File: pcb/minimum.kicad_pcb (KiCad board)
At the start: 4 copper layers, 16 x 20 mm, 31 parts, among them J1 DX07P024MJ1R1500, U1 RP2040, U2 SCD4x, U3 W25Q16JVUXIQ, U4 XCL220, Y1 C2E-12.000-18-1020-X-R

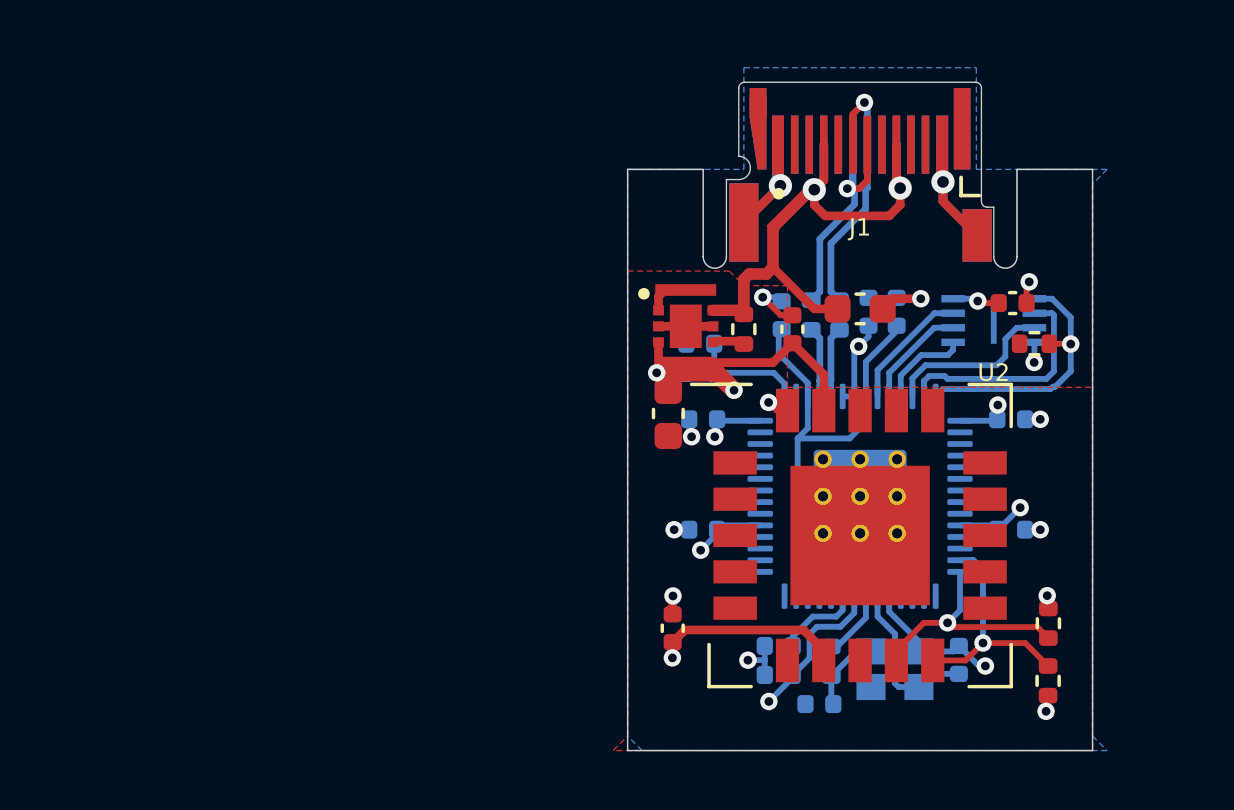
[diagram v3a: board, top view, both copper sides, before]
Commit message: adding led and push button libs
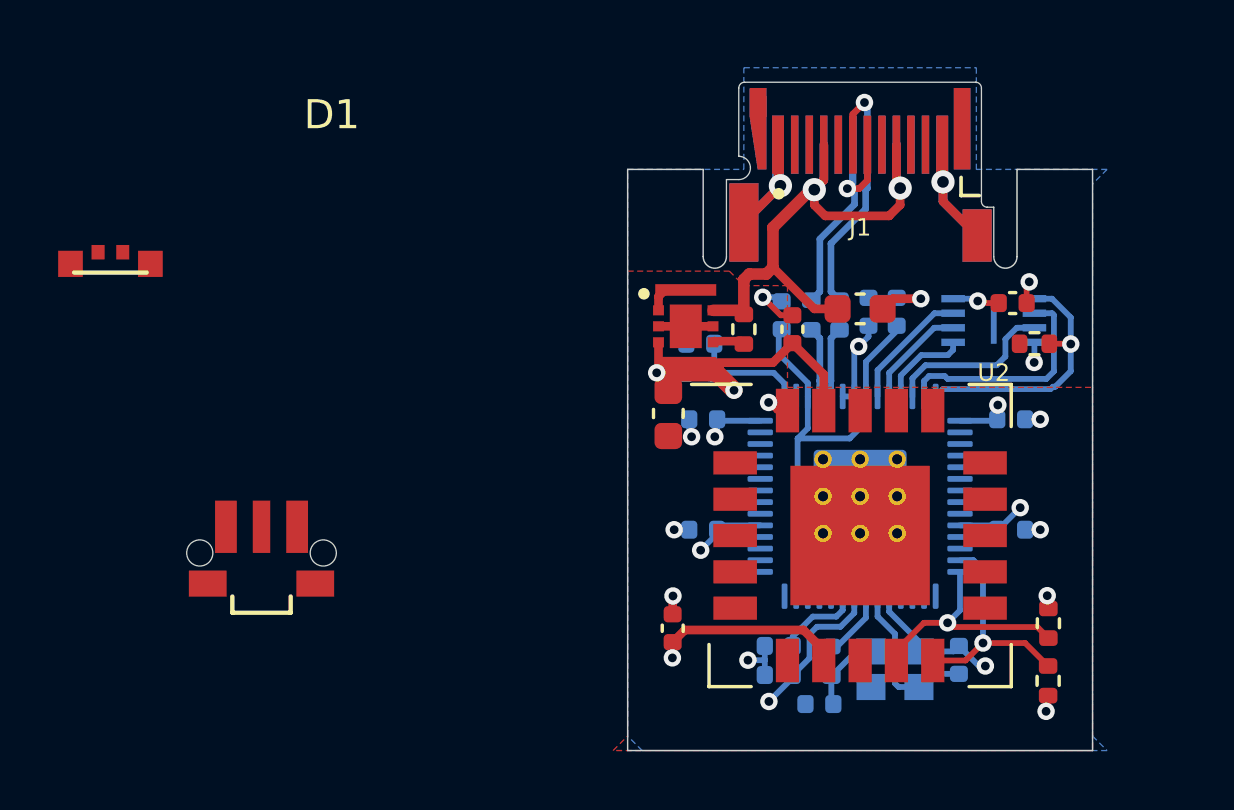
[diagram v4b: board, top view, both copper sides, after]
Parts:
- added D1: LED_BARG, SMD:RGB_LED_3x1, F.Cu at (74.2, 63.2)
- added SW1: SW_Push, SMD:TL3340AF160QG, F.Cu at (79.4, 73.2)
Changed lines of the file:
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@@
       (layer "F.Mask" (type "Top Solder Mask") (color "Green") (thickness 0.01))
       (layer "F.Cu" (type "copper") (thickness 0.035))
-      (layer "dielectric 1" (type "prepreg") (thickness 0.2 locked))
+      (layer "dielectric 1" (type "prepreg") (thickness 0.2 locked) (material "FR4") (epsilon_r 4.5) (loss_tangent 0.02))
       (layer "In1.Cu" (type "copper") (thickness 0.0175))
       (layer "dielectric 2" (type "core") (thickness 0.265 locked) (material "FR4") (epsilon_r 4.5) (loss_tangent 0.02))
       (layer "In2.Cu" (type "copper") (thickness 0.0175))
-      (layer "dielectric 3" (type "prepreg") (thickness 0.2 locked))
+      (layer "dielectric 3" (type "prepreg") (thickness 0.2 locked) (material "FR4") (epsilon_r 4.5) (loss_tangent 0.02))
       (layer "B.Cu" (type "copper") (thickness 0.035))
       (layer "B.Mask" (type "Bottom Solder Mask") (color "Green") (thickness 0.01))
@@
   (net 20 "/Pi_USB_D-")
   (net 21 "VBUS")
+  (net 22 "unconnected-(SW1-Pad2)")
+  (net 23 "unconnected-(D1-Pad1)")
+  (net 24 "unconnected-(D1-Pad2)")
+  (net 25 "unconnected-(D1-Pad3)")
+  (net 26 "unconnected-(D1-Pad4)")
   (footprint "SMD:QFN-20_EP_10.1x10.1_Pitch1.25mm" (layer "F.Cu")
     (at 100 72.6)
@@
     )
   )
+  (footprint "SMD:RGB_LED_3x1" (layer "F.Cu")
+    (at 74.2 63.2)
+    (property "Sheetfile" "minimum.kicad_sch")
+    (property "Sheetname" "")
+    (fp_text reference "D1" (at 7.62 -5.08) (layer "F.SilkS")
+      (effects (font (size 1 1) (thickness 0.15)))
+    )
+    (fp_text value "LED_BARG" (at 0 -5.08) (layer "F.Fab")
+      (effects (font (size 1 1) (thickness 0.15)))
+    )
+    (fp_line (start -1.25 0.35) (end 1.25 0.35) (layer "F.SilkS") (width 0.15))
+    (pad "1" smd rect (at 1.375 0.05) (size 0.85 0.9) (layers "F.Cu" "F.Paste" "F.Mask")
+      (net 23 "unconnected-(D1-Pad1)") (pinfunction "BK") (pintype "passive"))
+    (pad "2" smd rect (at 0.425 -0.35) (size 0.45 0.5) (layers "F.Cu" "F.Paste" "F.Mask")
+      (net 24 "unconnected-(D1-Pad2)") (pinfunction "A") (pintype "passive"))
+    (pad "3" smd rect (at -0.425 -0.35) (size 0.45 0.5) (layers "F.Cu" "F.Paste" "F.Mask")
+      (net 25 "unconnected-(D1-Pad3)") (pinfunction "RK") (pintype "passive"))
+    (pad "4" smd rect (at -1.375 0.05) (size 0.85 0.9) (layers "F.Cu" "F.Paste" "F.Mask")
+      (net 26 "unconnected-(D1-Pad4)") (pinfunction "GK") (pintype "passive"))
+    (model "${KIPRJMOD}/3Dshapes/APFA2507.step"
+      (offset (xyz 0 0 0))
+      (scale (xyz 1 1 1))
+      (rotate (xyz 0 0 0))
+    )
+  )
   (footprint "Resistor_SMD:R_0402_1005Metric" (layer "F.Cu")
     (at 106.48 75.62 -90)
@@
     )
   )
+  (footprint "SMD:TL3340AF160QG" (layer "F.Cu")
+    (at 79.4 73.2)
+    (property "Sheetfile" "minimum.kicad_sch")
+    (property "Sheetname" "")
+    (attr smd)
+    (fp_text reference "SW1" (at 2.46126 2.37744) (layer "F.Fab")
+      (effects (font (size 0.6 0.6) (thickness 0.15)))
+    )
+    (fp_text value "SW_Push" (at 0.74 -3.29) (layer "F.Fab")
+      (effects (font (size 1 1) (thickness 0.15)))
+    )
+    (fp_line (start -1.0033 1.495552) (end -1.0033 2.0574) (layer "F.SilkS") (width 0.15))
+    (fp_line (start 1.0033 1.495552) (end 1.0033 2.0574) (layer "F.SilkS") (width 0.15))
+    (fp_line (start -1.0033 2.0574) (end 1.0033 2.0574) (layer "F.SilkS") (width 0.15))
+    (pad "" np_thru_hole circle (at 2.125 0) (size 0.9 0.9) (drill 0.9) (layers *.Cu *.Mask))
+    (pad "" np_thru_hole circle (at -2.125 0) (size 0.9 0.9) (drill 0.9) (layers *.Cu *.Mask))
+    (pad "1" smd rect (at -1.225 -0.9) (size 0.75 1.8) (layers "F.Cu" "F.Paste" "F.Mask")
+      (pinfunction "1") (pintype "passive"))
+    (pad "2" smd rect (at -1.85 1.0541) (size 1.3 0.9) (layers "F.Cu" "F.Paste" "F.Mask")
+      (net 22 "unconnected-(SW1-Pad2)") (pinfunction "2") (pintype "passive"))
+    (pad "2" smd rect (at 0 -0.9017) (size 0.6 1.8) (layers "F.Cu" "F.Paste" "F.Mask")
+      (net 22 "unconnected-(SW1-Pad2)") (pinfunction "2") (pintype "passive"))
+    (pad "2" smd rect (at 1.85 1.0541) (size 1.3 0.9) (layers "F.Cu" "F.Paste" "F.Mask")
+      (net 22 "unconnected-(SW1-Pad2)") (pinfunction "2") (pintype "passive"))
+    (pad "3" smd rect (at 1.225 -0.9) (size 0.75 1.8) (layers "F.Cu" "F.Paste" "F.Mask"))
+    (model "${KIPRJMOD}/3dshapes/TL3340AF160QG.step"
+      (offset (xyz 0 1.33349998 1.650999975))
+      (scale (xyz 1 1 1))
+      (rotate (xyz 90 0 -180))
+    )
+    (model "${KIPRJMOD}/3Dshapes/TL3340AF160QG.step"
+      (offset (xyz 0 1.4 1.5))
+      (scale (xyz 1 1 1))
+      (rotate (xyz 90 0 180))
+    )
+  )

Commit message: routing
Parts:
- added R10: 470, Resistor_SMD:R_0402_1005Metric, B.Cu at (93.8, 74.0)
- added R8: 470, Resistor_SMD:R_0402_1005Metric, B.Cu at (93.8, 71.5)
- added R9: 470, Resistor_SMD:R_0402_1005Metric, B.Cu at (93.8, 70.5)
- moved SW1 29.0 mm to (107.2, 65.0), turned to 90 degrees
- moved D1 20.5 mm to (92.6, 72.2), turned to -90 degrees
- moved R6 2.24 mm to (103.8, 65.8), turned to 180 degrees
- moved C16 1.49 mm to (103.8, 64.4)
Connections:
- D1 pad 1: unconnected-(D1-Pad1) -> Net-(R10-Pad2)
- D1 pad 2: unconnected-(D1-Pad2) -> GND
- D1 pad 3: unconnected-(D1-Pad3) -> Net-(D1-Pad3)
- D1 pad 4: unconnected-(D1-Pad4) -> Net-(D1-Pad4)
- R6 pad 1: (no net) -> Net-(R6-Pad1)
- SW1 pad 1: (no net) -> GND
- SW1 pad 2: unconnected-(SW1-Pad2) -> Net-(R6-Pad1)
- U1 pad 32: (no net) -> /LED_B
- U1 pad 34: (no net) -> /LED_R
- U1 pad 35: (no net) -> /LED_G
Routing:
- net Net-(R6-Pad1): track 0.00 -> 9.02 mm
- net /LED_B: track 0.00 -> 2.84 mm
- net /LED_G: track 0.00 -> 2.75 mm
- net GND: track 34.4 -> 36.9 mm, vias 14 -> 12
- net /LED_R: track 0.00 -> 2.41 mm
- net Net-(D1-Pad4): track 0.00 -> 1.25 mm, vias 0 -> 1
- net Net-(R10-Pad2): track 0.00 -> 1.19 mm, vias 0 -> 1
- net Net-(D1-Pad3): track 0.00 -> 1.14 mm, vias 0 -> 1
- net /QSPI_SS: track 9.12 -> 9.85 mm, vias 1 -> 2
- net +3V3: track 43.4 -> 42.7 mm
- net /QSPI_SD1: track 7.85 -> 7.33 mm
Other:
- board size 16 x 20 mm -> 17 x 20 mm

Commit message: RC
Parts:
- moved R4 0.12 mm to (106.4, 77.5)
- moved R3 0.08 mm to (106.4, 75.6)
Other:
- outline, holes or cut-outs redrawn
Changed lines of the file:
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@@
   (net 23 "Net-(D1-Pad3)")
   (net 24 "Net-(D1-Pad4)")
-  (net 25 "Net-(R10-Pad2)")
+  (net 25 "Net-(D1-Pad1)")
   (net 26 "/LED_R")
   (net 27 "/LED_G")
@@
   )
   (footprint "Resistor_SMD:R_0402_1005Metric" (layer "F.Cu")
-    (at 106.47 77.6 90)
+    (at 106.4 77.5 90)
     (descr "Resistor SMD 0402 (1005 Metric), square (rectangular) end terminal, IPC_7351 nominal, (Body size source: IPC-SM-782 page 72, https://www.pcb-3d.com/wordpress/wp-content/uploads/ipc-sm-782a_amendment_1_and_2.pdf), generated with kicad-footprint-generator")
     (tags "resistor")
@@
     (fp_line (start -1.25 0.35) (end 1.25 0.35) (layer "F.SilkS") (width 0.15))
     (pad "1" smd rect (at 1.375 0.05 270) (size 0.85 0.9) (layers "F.Cu" "F.Paste" "F.Mask")
-      (net 25 "Net-(R10-Pad2)") (pinfunction "BK") (pintype "passive"))
+      (net 25 "Net-(D1-Pad1)") (pinfunction "BK") (pintype "passive"))
     (pad "2" smd rect (at 0.425 -0.35 270) (size 0.45 0.5) (layers "F.Cu" "F.Paste" "F.Mask")
       (net 3 "GND") (pinfunction "A") (pintype "passive"))
@@
   )
   (footprint "Resistor_SMD:R_0402_1005Metric" (layer "F.Cu")
-    (at 106.48 75.62 -90)
+    (at 106.4 75.62 -90)
     (descr "Resistor SMD 0402 (1005 Metric), square (rectangular) end terminal, IPC_7351 nominal, (Body size source: IPC-SM-782 page 72, https://www.pcb-3d.com/wordpress/wp-content/uploads/ipc-sm-782a_amendment_1_and_2.pdf), generated with kicad-footprint-generator")
     (tags "resistor")
@@
       (net 28 "/LED_B") (pintype "passive"))
     (pad "2" smd roundrect locked (at 0.51 0 180) (size 0.54 0.64) (layers "B.Cu" "B.Paste" "B.Mask") (roundrect_rratio 0.25)
-      (net 25 "Net-(R10-Pad2)") (pintype "passive"))
+      (net 25 "Net-(D1-Pad1)") (pintype "passive"))
     (model "${KISYS3DMOD}/Resistor_SMD.3dshapes/R_0402_1005Metric.wrl"
       (offset (xyz 0 0 0))
@@
       (effects (font (size 1 1) (thickness 0.15)) (justify mirror))
     )
-    (fp_text value "W25Q16JVUXIQ" (at -0.62 3.25) (layer "B.SilkS")
+    (fp_text value "W25Q16JVUXIQ" (at -0.62 3.25) (layer "B.SilkS") hide
       (effects (font (size 1 1) (thickness 0.15)) (justify mirror))
     )
@@
   (gr_arc (start 95 63) (end 95.4 63) (angle 180) (layer "Edge.Cuts") (width 0.05))
   (gr_arc (start 105 63) (end 105.4 63) (angle 180) (layer "Edge.Cuts") (width 0.05))
+  (gr_line (start 92 79) (end 92 80) (layer "Edge.Cuts") (width 0.05))
+  (gr_arc (start 108 78) (end 108 79) (angle 180) (layer "Edge.Cuts") (width 0.05))
+  (gr_arc (start 92 78) (end 92 77) (angle 180) (layer "Edge.Cuts") (width 0.05))
   (gr_line (start 108 61) (end 108 60) (layer "Edge.Cuts") (width 0.05))
   (gr_line (start 109 62) (end 109 68) (layer "Edge.Cuts") (width 0.05))
   (gr_arc (start 109 61.000003) (end 109 62) (angle 90) (layer "Edge.Cuts") (width 0.05))
   (gr_line (start 105.4 63) (end 105.4 60) (layer "Edge.Cuts") (width 0.05))
-  (gr_line (start 108 69) (end 108 80) (layer "Edge.Cuts") (width 0.05))
-  (gr_line (start 92 80) (end 92 60) (layer "Edge.Cuts") (width 0.05))
+  (gr_line (start 108 69) (end 108 77) (layer "Edge.Cuts") (width 0.05))
+  (gr_line (start 92 77) (end 92 60) (layer "Edge.Cuts") (width 0.05))
   (gr_line (start 92 60) (end 94.6 60) (layer "Edge.Cuts") (width 0.05))
+  (gr_line (start 108 79) (end 108 80) (layer "Edge.Cuts") (width 0.05))
   (gr_arc (start 108.999997 69) (end 108 69) (angle 90) (layer "Edge.Cuts") (width 0.05))
   (gr_line (start 94.6 60) (end 94.6 63) (layer "Edge.Cuts") (width 0.05))
   (dimension (type aligned) (layer "Cmts.User")
-    (pts (xy 96 80) (xy 96 47.3375))
-    (height -5.5)
-    (gr_text "32,6625 mm" (at 89.35 63.66875 90) (layer "Cmts.User")
-      (effects (font (size 1 1) (thickness 0.15)))
-    )
+    (pts (xy 92 80) (xy 92 48))
+    (height -2.75)
+    (gr_text "32,0000 mm" (at 88.1 64 90) (layer "Cmts.User")
+      (effects (font (size 1 1) (thickness 0.15)))
+    )

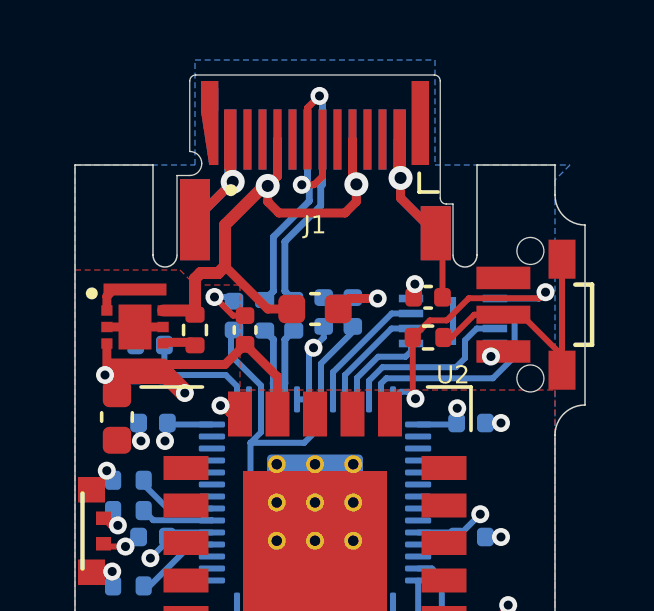
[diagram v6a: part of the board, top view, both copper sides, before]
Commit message: OH logo added
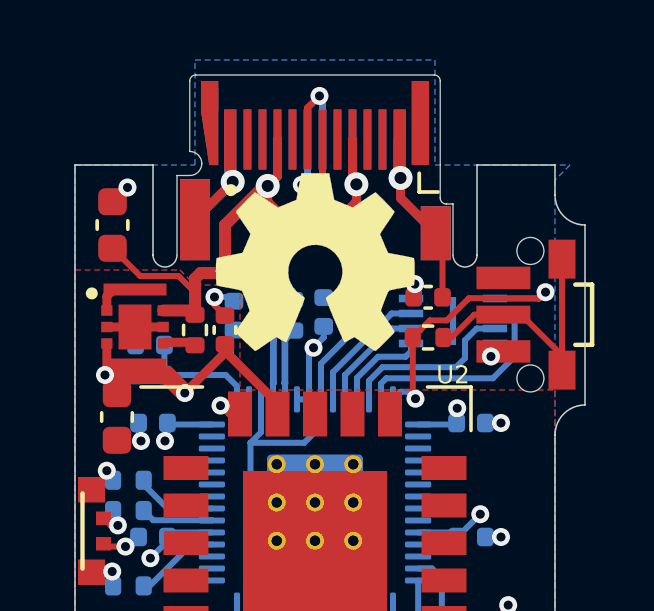
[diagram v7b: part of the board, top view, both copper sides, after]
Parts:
- added REF**: OSHW-Symbol_6.7x6mm_SilkScreen, Symbol:OSHW-Symbol_6.7x6mm_SilkScreen, F.Cu at (100.0, 63.2)
- moved C17 7.31 mm to (93.2, 62.0), turned to 90 degrees
- moved C8 0.67 mm to (97.0, 65.5)
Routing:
- net GND: track 36.9 -> 34.8 mm
- net +3V3: track 42.7 -> 41.2 mm
- net VBUS: track 20.5 -> 21.0 mm

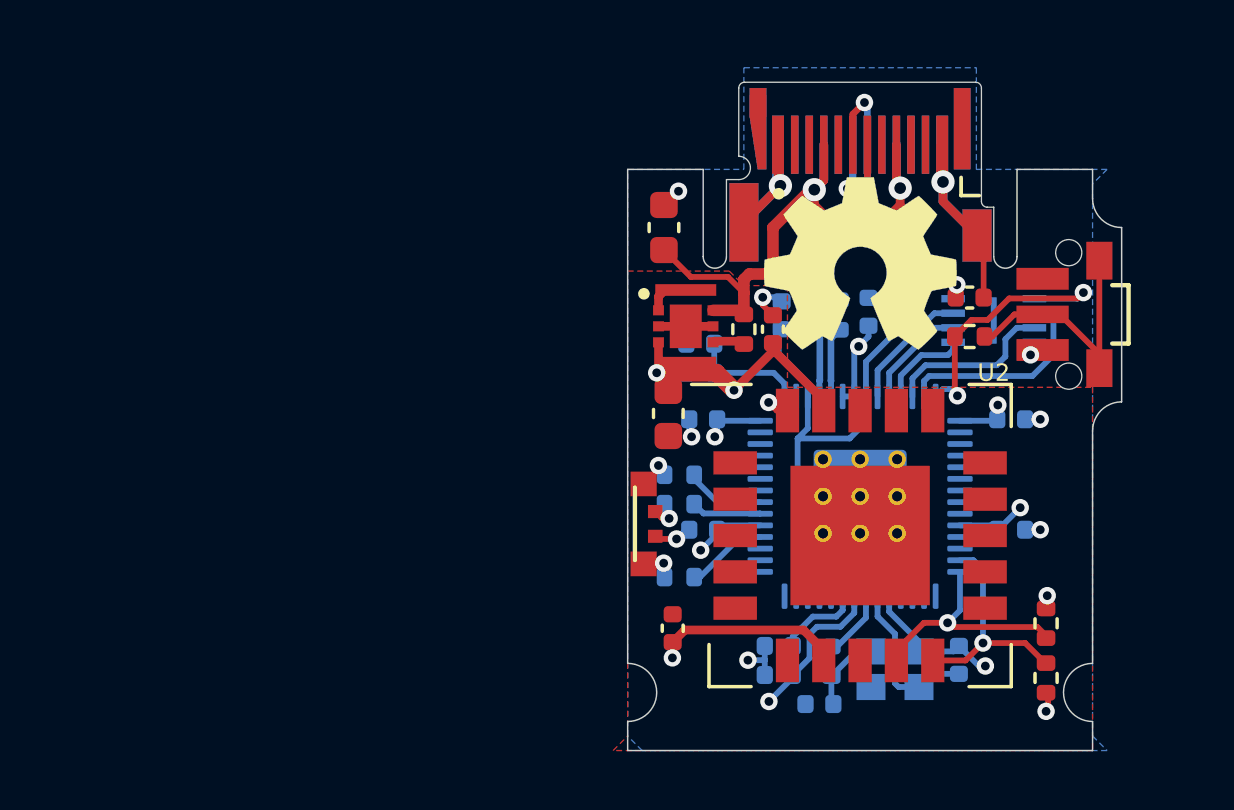
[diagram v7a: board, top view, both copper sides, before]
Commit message: changing the USB connector following the recommendation of arturo182
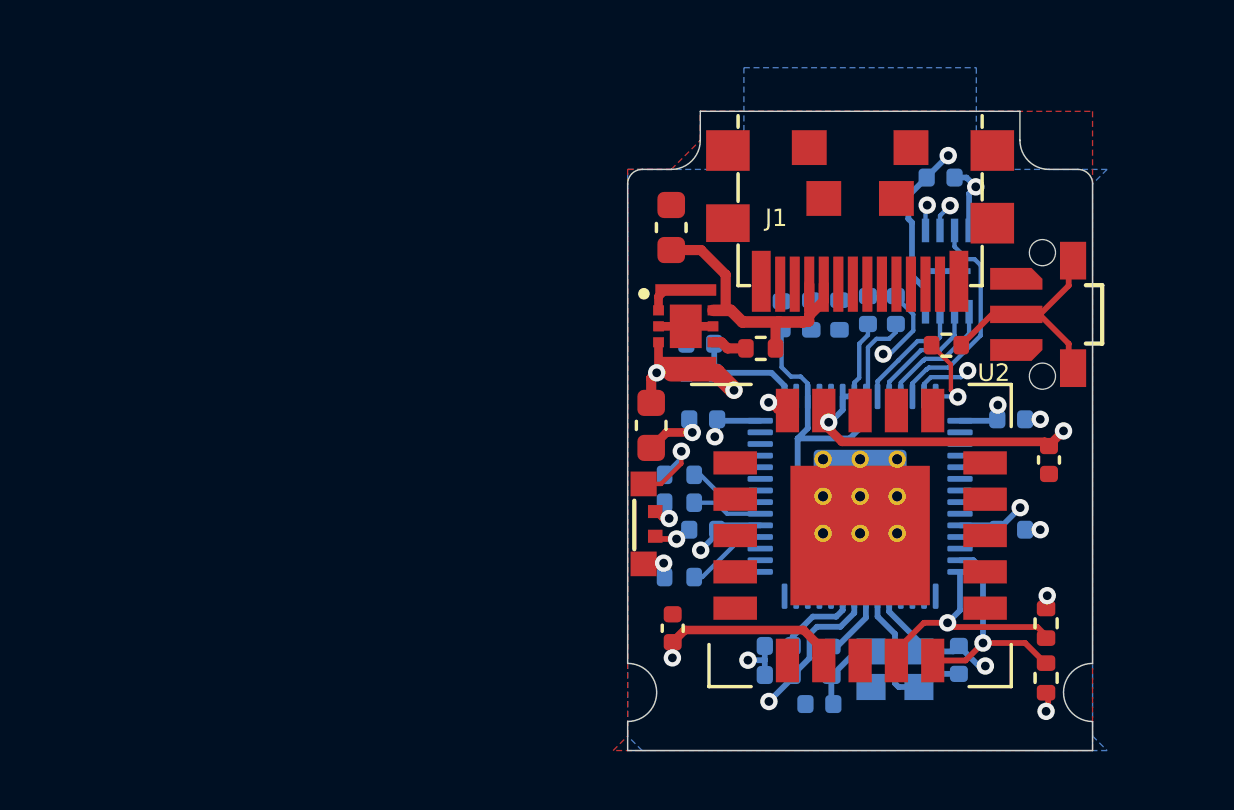
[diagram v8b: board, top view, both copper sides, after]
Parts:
- removed REF**: OSHW-Symbol_6.7x6mm_SilkScreen, Symbol:OSHW-Symbol_6.7x6mm_SilkScreen
- C16: moved to B.Cu
- J1: footprint SMD:JAE_DX07P024MJ1R1500 -> SMD:USB_C_Plug_UTC009-C12
- moved C8 10.5 mm to (106.5, 70.0), turned to -90 degrees
- moved J1 6.75 mm to (100.0, 63.8)
- moved C16 4.25 mm to (102.8, 60.3)
- moved U3 2.33 mm to (103.0, 63.5), turned to -90 degrees
- moved SW1 0.91 mm to (106.3, 65.0)
- moved R7 0.88 mm to (96.6, 66.2), turned to 180 degrees
- moved R6 0.85 mm to (103.0, 66.0)
- moved C18 0.72 mm to (92.8, 68.8)
- moved C17 0.25 mm to (93.5, 62.0)
- moved C12 0.07 mm to (101.2, 64.8)
- moved C6 0.06 mm to (100.3, 64.8)
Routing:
- net GND: track 34.8 -> 21.9 mm, vias 12 -> 9
- net VBUS: track 21.0 -> 10.9 mm, vias 2 -> 0
- net +3V3: track 41.2 -> 51.0 mm, vias 12 -> 13
- net /USB_D-: track 9.62 -> 0.00 mm, vias 1 -> 0
- net /USB_D+: track 9.10 -> 0.00 mm, vias 1 -> 0
- net /Pi_USB_D-: track 2.42 -> 0.00 mm
- net /Pi_USB_D+: track 2.42 -> 0.00 mm
- net Net-(R6-Pad1): track 9.02 -> 6.97 mm
- net Net-(D1-Pad4): track 1.25 -> 3.06 mm
- net /QSPI_SD2: track 5.89 -> 7.62 mm
- net /QSPI_SD1: track 7.33 -> 9.04 mm, vias 0 -> 2
- net /QSPI_SD0: track 3.14 -> 4.28 mm
- net /QSPI_SS: track 9.85 -> 10.9 mm
- net +1V1: track 19.8 -> 20.4 mm
- net /QSPI_SCLK: track 3.66 -> 4.23 mm
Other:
- board size 17 x 20 mm -> 16 x 22 mm
